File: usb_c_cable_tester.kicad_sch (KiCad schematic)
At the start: 58 parts, among them J1 USB C, J2 USB C, J3 USB_B_Micro, J4 USB3_B, J5 USB_B_Mini, J6 USB3_A

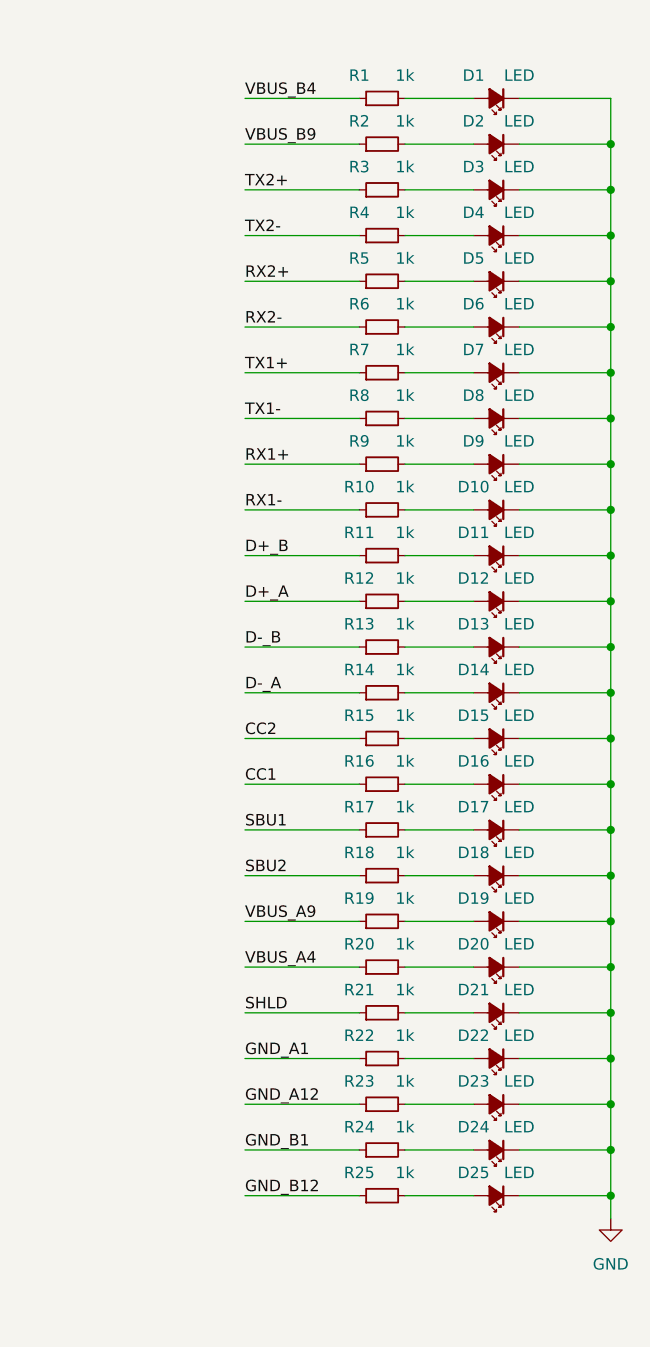
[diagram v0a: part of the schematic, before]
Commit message: v3.0. Vertical connectors, through hole where possible. #8, #19, #21, #36
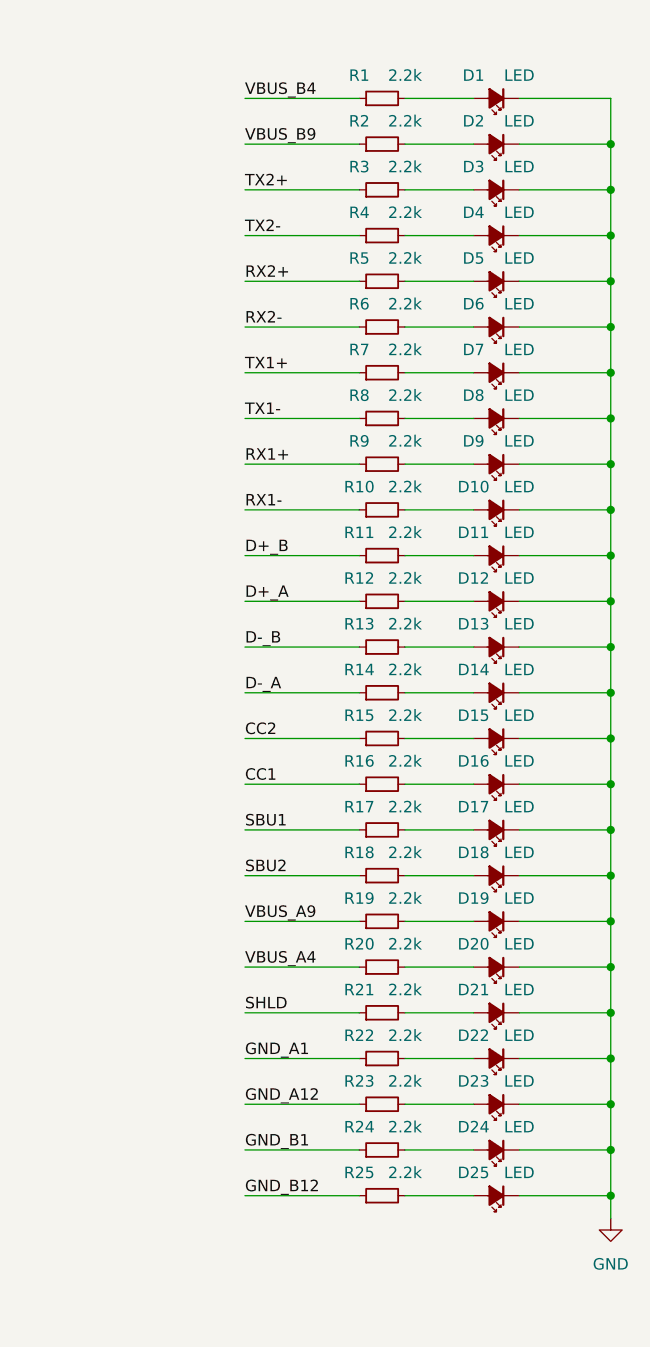
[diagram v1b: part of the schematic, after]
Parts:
- C1: footprint Capacitor_SMD:C_0805_2012Metric -> Capacitor_SMD:C_0805_2012Metric_Pad1.18x1.45mm_HandSolder
- D1, D10, D11, D12, D13, D14, D15, D16, D17, D18, D19, D2, D20, D21, D22, D23, D24, D25, D3, D4, D5, D6, D7, D8, D9: footprint LED_SMD:LED_0603_1608Metric -> LED_SMD:LED_0603_1608Metric_Pad1.05x0.95mm_HandSolder
- J1, J2: footprint Libraries:USB_C_Receptacle_24P_QCHT_C456013 -> Connector_USB:USB_C_Receptacle_JAE_DX07S024WJ3R400; Alt LCSC C2761408 -> (none); LCSC C456013 -> C2840387
- J3: footprint easyeda:MICRO-USB-SMD_10118194-0001LF -> Connector_USB:USB_Micro-B_Wuerth_614105150721_Vertical; Alt LCSC (none) -> C668588; LCSC C404969 -> C456007
- J4: footprint easyeda:USB-B-TH_XUNPU_USB-306BWD-ARW -> Libraries:USB_B_3.0_C2763106; LCSC C105423 -> C2763106
- J5: footprint easyeda:MINI-USB-SMD_MINI-5PTP -> Connector_USB:USB_Mini-B_Tensility_54-00023_Vertical; Alt LCSC (none) -> C720613, C6331167; LCSC C2681563 -> C13453
- J6: footprint easyeda:USB-A-TH_U231-091N-5 -> Libraries:USB_A_3.0_HC-USB3.0-L137-ZP_C19273972
- R1, R10, R11, R12, R13, R14, R15, R16, R17, R18, R19, R2, R20, R21, R22, R23, R24, R25, R3, R4, R5, R6, R7, R8, R9: value 1k -> 2.2k; footprint Resistor_SMD:R_0603_1608Metric -> Resistor_SMD:R_0603_1608Metric_Pad0.98x0.95mm_HandSolder

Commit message: Oops, missed the USB-A LCSC part number. Fixed. #36
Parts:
- J6: LCSC C381137 -> C19273972
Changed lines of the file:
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@@
 			)
 		)
-		(property "LCSC" "C381137"
+		(property "LCSC" "C19273972"
 			(at 167.64 110.49 0)
 			(effects
